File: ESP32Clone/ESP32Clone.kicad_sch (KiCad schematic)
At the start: 14 parts, among them J1 Connector, USB-TYPE-C-16P, U1 TPS54331DR

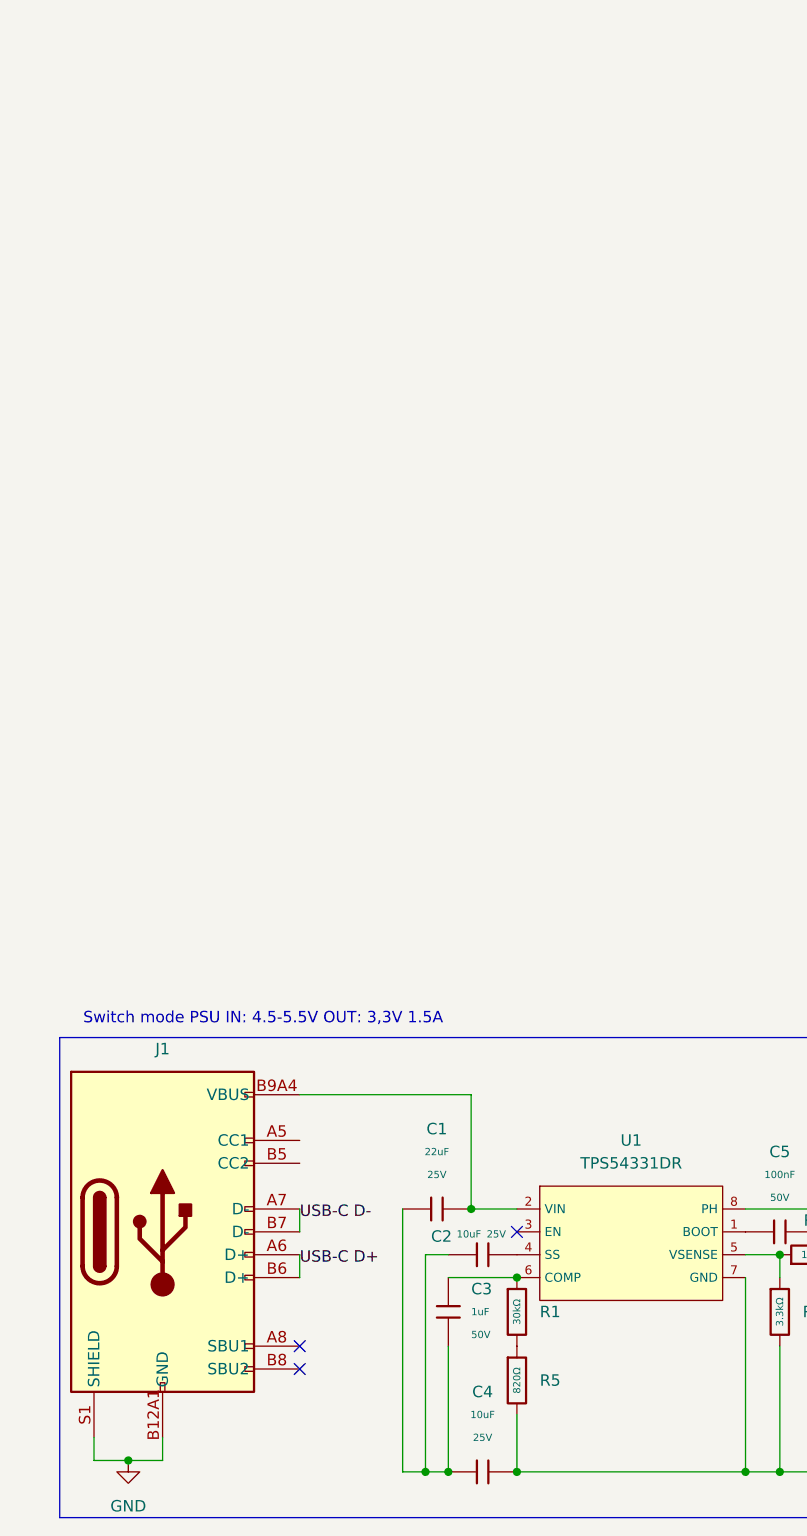
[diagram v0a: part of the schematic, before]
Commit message: connected configuration pins
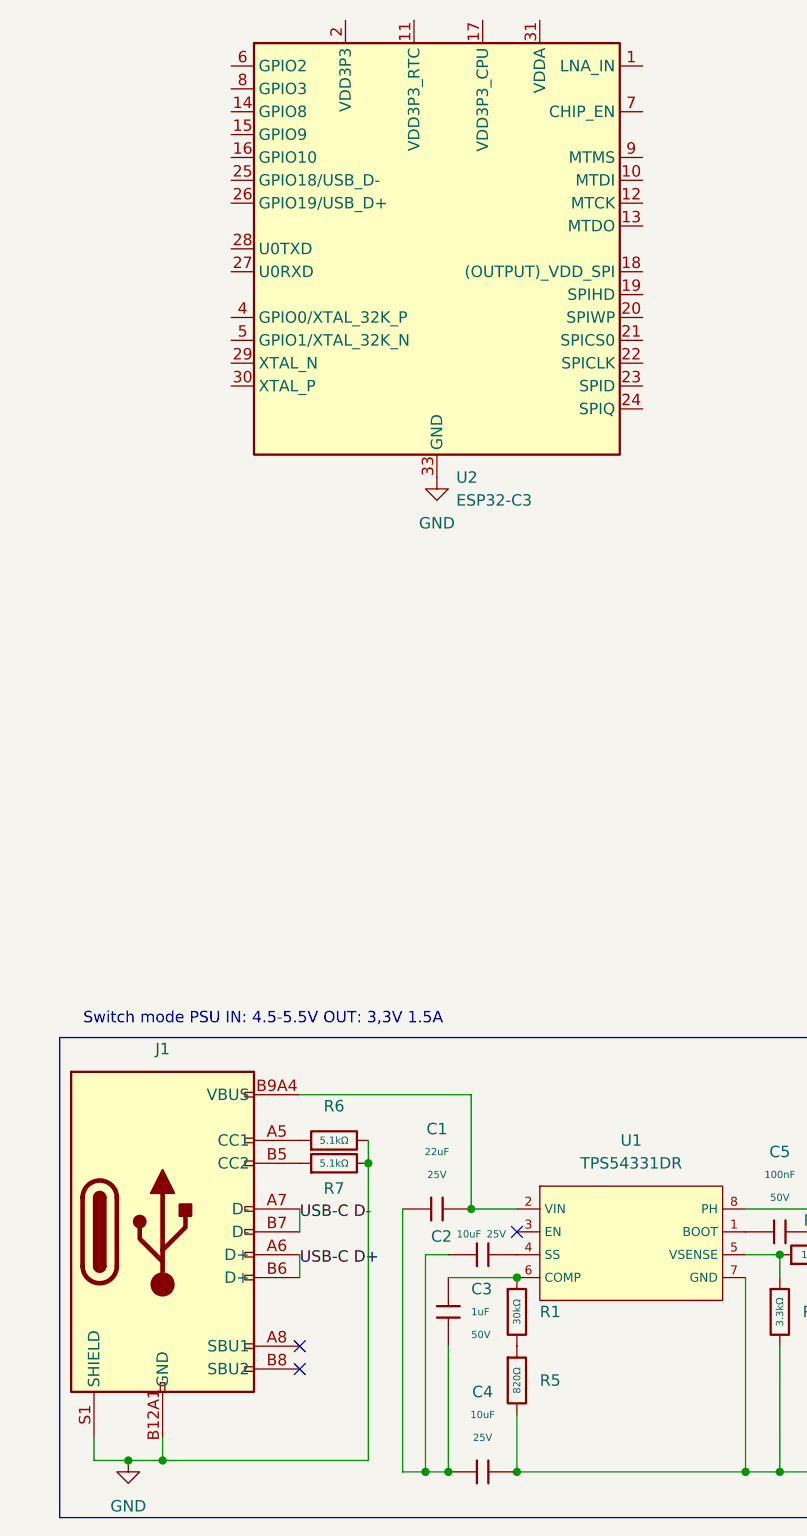
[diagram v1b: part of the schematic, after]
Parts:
- added R6, R7: 5.1kΩ, PCM_JLCPCB:R_0805, symbol PCM_JLCPCB-Resistors:0805,5.1kΩ
- added U2: ESP32-C3, PCM_JLCPCB:QFN-32-1EP_5x5mm_P0.5mm_EP3.7x3.7mm_ThermalVias, symbol PCM_JLCPCB-Extended:MCU, ESP32-C3
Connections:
- net GND: now also R6.2, R7.2, U2.33 (GND)
- net at J1.A5 (CC1): now also R6.1
- net at J1.B5 (CC2): now also R7.1
- new net: U2.2 (VDD3P3), U2.3 (VDD3P3)
- new net: U2.31 (VDDA), U2.32 (VDDA)

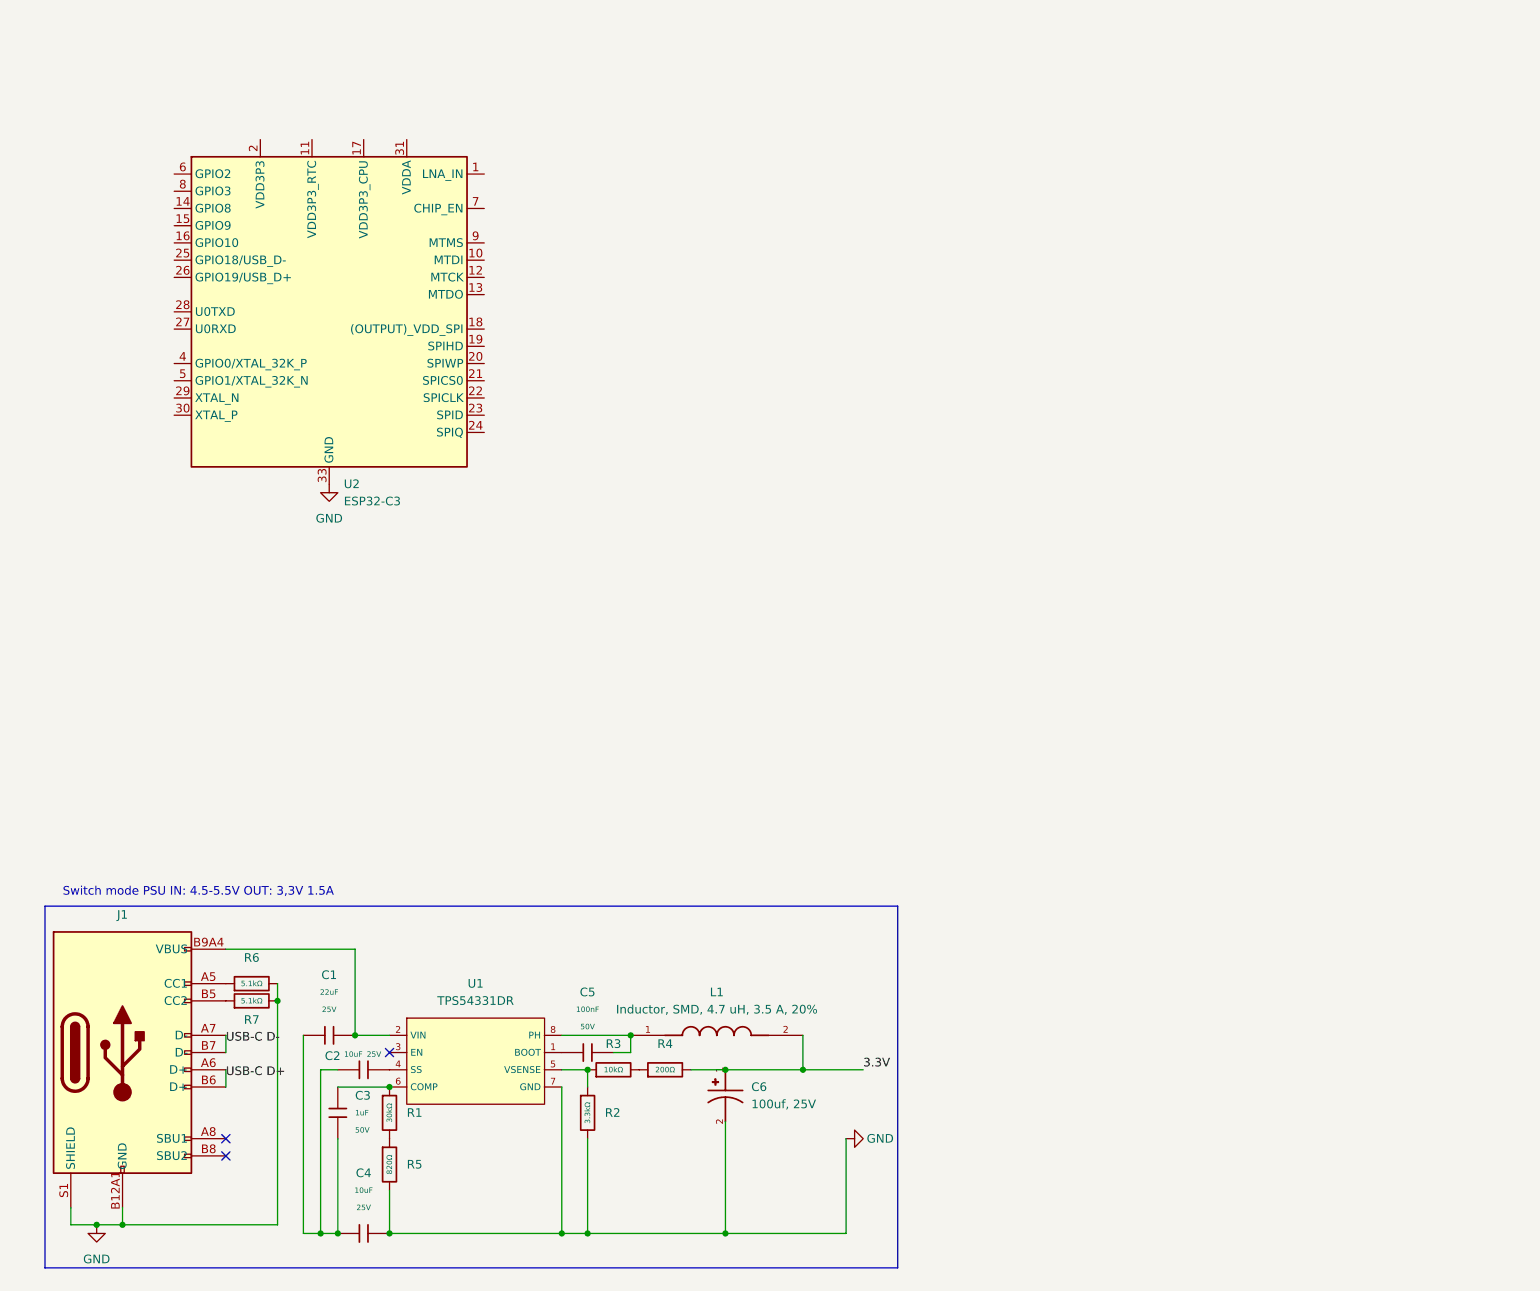
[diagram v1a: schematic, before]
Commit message: ESP 32 added
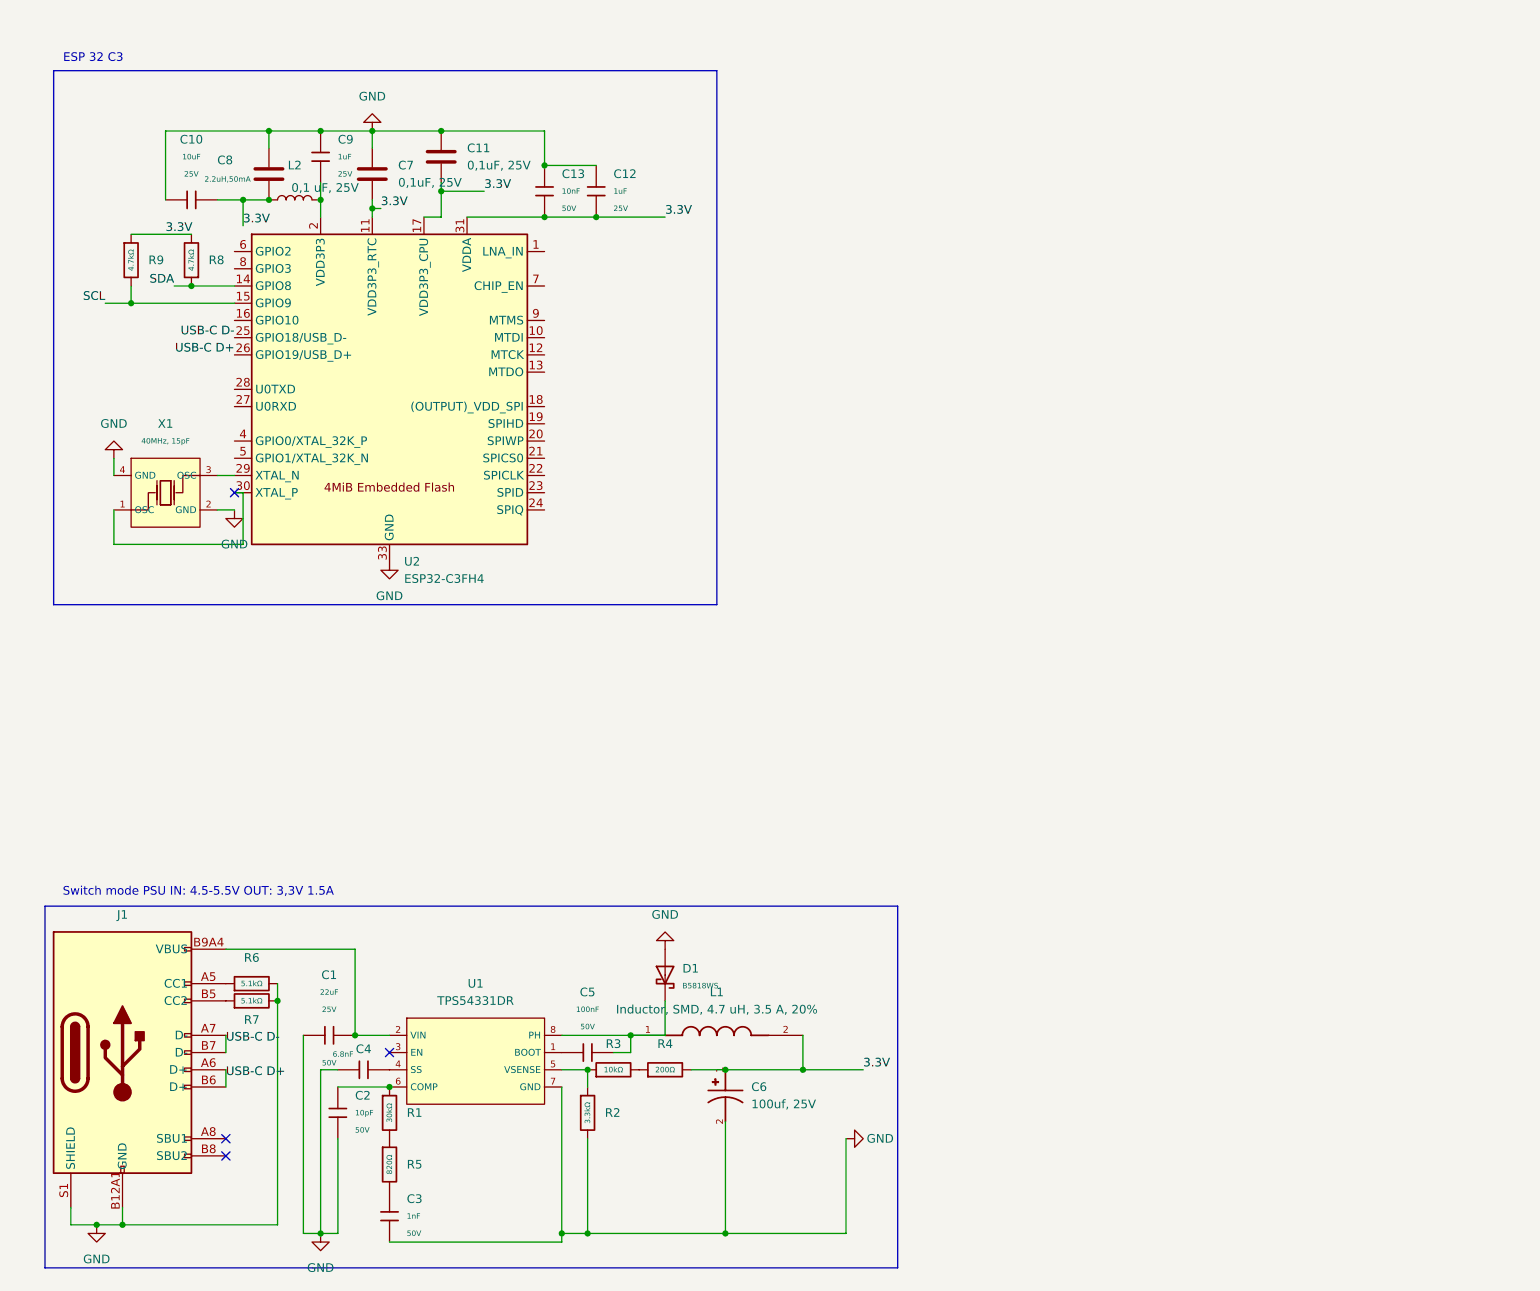
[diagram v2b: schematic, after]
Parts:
- removed C2, C4: 10uF, PCM_JLCPCB:C_0805, symbol PCM_JLCPCB-Capacitors:0805,10uF
- removed C3: 1uF, PCM_JLCPCB:C_0603, symbol PCM_JLCPCB-Capacitors:0603,1uF
- removed U2: ESP32-C3, PCM_JLCPCB:QFN-32-1EP_5x5mm_P0.5mm_EP3.7x3.7mm_ThermalVias, symbol PCM_JLCPCB-Extended:MCU, ESP32-C3
- added C10: 10uF, PCM_JLCPCB:C_0603, symbol PCM_JLCPCB-Capacitors:0603,10uF,(2)
- added C11, C7: 0,1uF, 25V, symbol Device:C
- added C12, C9: 1uF, PCM_JLCPCB:C_0402, symbol PCM_JLCPCB-Capacitors:0402,1uF
- added C13: 10nF, PCM_JLCPCB:C_0402, symbol PCM_JLCPCB-Capacitors:0402,10nF
- added C2: 10pF, PCM_JLCPCB:C_0402, symbol PCM_JLCPCB-Capacitors:0402,10pF
- added C3: 1nF, PCM_JLCPCB:C_0402, symbol PCM_JLCPCB-Capacitors:0402,1nF
- added C4: 6.8nF, PCM_JLCPCB:C_0402, symbol PCM_JLCPCB-Capacitors:0402,6.8nF
- added C8: 0,1 uF, 25V, symbol Device:C
- added D1: B5818WS, PCM_JLCPCB:D_SOD-323, symbol PCM_JLCPCB-Diodes:Schottky,B5818WS
- added L2: 2.2uH,50mA, PCM_JLCPCB:L_0805, symbol PCM_JLCPCB-Inductors:2.2uH,50mA
- added R8, R9: 4.7kΩ, PCM_JLCPCB:R_0805, symbol PCM_JLCPCB-Resistors:0805,4.7kΩ
- added U2: ESP32-C3FH4, PCM_JLCPCB:QFN-32-1EP_5x5mm_P0.5mm_EP3.7x3.7mm_ThermalVias, symbol PCM_JLCPCB-Extended:MCU, ESP32-C3FH4
- added X1: 40MHz, 15pF, PCM_JLCPCB:OSC-SMD_4P-L3.2-W2.5-BL_SIT8008BI, symbol PCM_JLCPCB-Extended:Crystal, 40MHz, 15pF
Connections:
- net 3.3V: now also C10.2, C11.2, C12.1, C13.2, C7.2, C8.2, L2.1, R8.2, R9.1, U2.11 (VDD3P3_RTC), U2.17 (VDD3P3_CPU), U2.31 (VDDA), U2.32 (VDDA)
- net GND: now also C1.1, C10.1, C11.1, C12.2, C13.1, C2.2, C3.1, C4.1, C7.1, C8.1, C9.1, D1.2, U2.33 (GND), X1.2 (GND), X1.4 (GND); no longer R5.2
- net USB-C D+: now also U2.26 (GPIO19/USB_D+)
- net USB-C D-: now also U2.25 (GPIO18/USB_D-)
- net at U1.4 (SS): now also C4.2
- net at R1.1, U1.6 (COMP): now also C2.1
- net at C5.1, L1.1, U1.8 (PH): now also D1.1
- new net: C3.2, R5.2
- new net: C9.2, L2.2, U2.2 (VDD3P3), U2.3 (VDD3P3)
- new net: U2.29 (XTAL_N), X1.3 (OSC)
- new net: U2.30 (XTAL_P), X1.1 (OSC)
- new net SCL: R9.2, U2.15 (GPIO9)
- new net SDA: R8.1, U2.14 (GPIO8)
- no-connect marks 3 -> 4
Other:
- note added: "ESP 32 C3"

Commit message: Further work on connectors
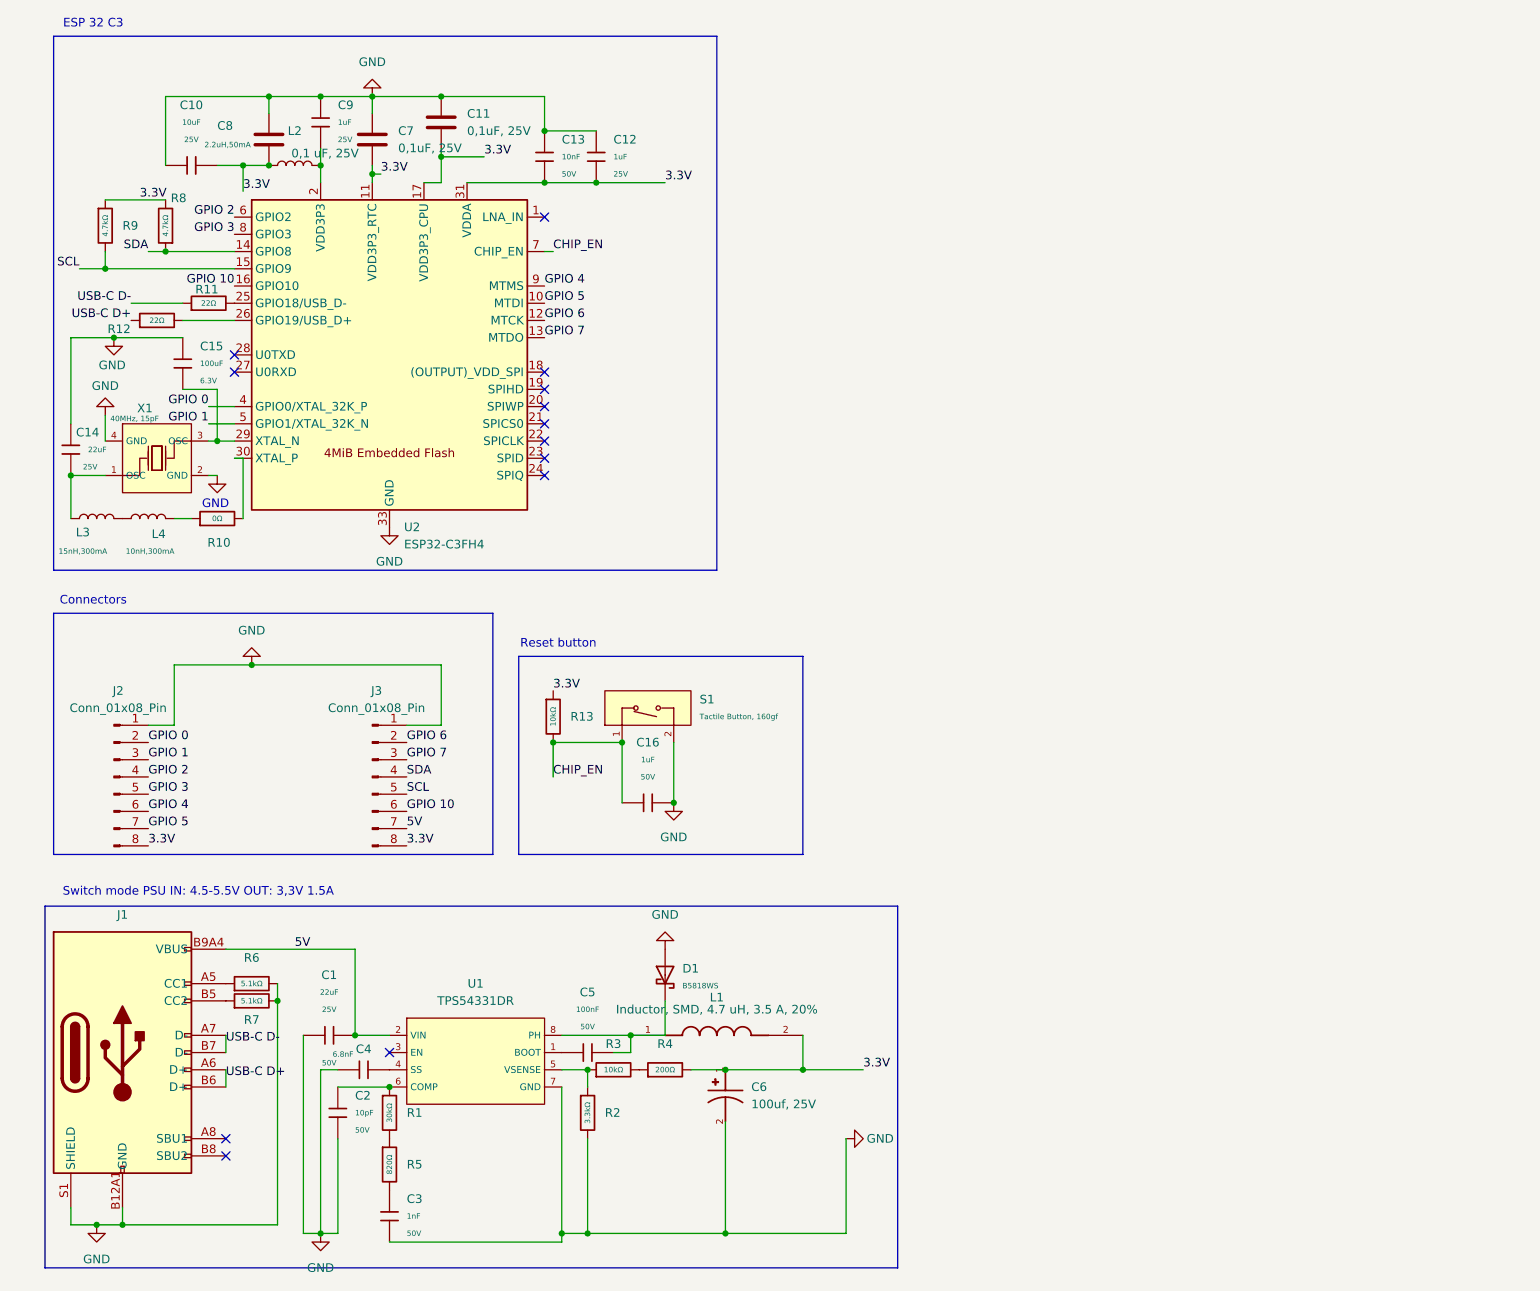
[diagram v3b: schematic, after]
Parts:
- added C14: 22uF, PCM_JLCPCB:C_0805, symbol PCM_JLCPCB-Capacitors:0805,22uF
- added C15: 100uF, PCM_JLCPCB:C_1206, symbol PCM_JLCPCB-Capacitors:1206,100uF
- added C16: 1uF, PCM_JLCPCB:C_0603, symbol PCM_JLCPCB-Capacitors:0603,1uF
- added J2, J3: Conn_01x08_Pin, symbol Connector:Conn_01x08_Pin
- added L3: 15nH,300mA, PCM_JLCPCB:L_0402, symbol PCM_JLCPCB-Inductors:15nH,300mA
- added L4: 10nH,300mA, PCM_JLCPCB:L_0402, symbol PCM_JLCPCB-Inductors:10nH,300mA
- added R10: 0Ω, PCM_JLCPCB:R_0805, symbol PCM_JLCPCB-Resistors:0805,0Ω
- added R11, R12: 22Ω, PCM_JLCPCB:R_0805, symbol PCM_JLCPCB-Resistors:0805,22Ω
- added R13: 10kΩ, PCM_JLCPCB:R_0603, symbol PCM_JLCPCB-Resistors:0603,10kΩ
- added S1: Tactile Button, 160gf, PCM_JLCPCB:SW_TS-1088-AR02016, symbol PCM_JLCPCB-Connectors_Buttons:Tactile Button, 160gf, 12V, 50mA, 4.0mm
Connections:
- net 3.3V: now also J2.8 (Pin_8), J3.8 (Pin_8), R13.1
- net GND: now also C14.1, C15.2, C16.2, J2.1 (Pin_1), J3.1 (Pin_1), S1.2 (B)
- net SCL: now also J3.5 (Pin_5)
- net SDA: now also J3.4 (Pin_4)
- net USB-C D+: now also R12.1; no longer U2.26 (GPIO19/USB_D+)
- net USB-C D-: now also R11.1; no longer U2.25 (GPIO18/USB_D-)
- net 5V: now reaches C1.2, J1.A9B4 (VBUS), J1.B9A4 (VBUS), U1.2 (VIN)
- net 5V: now also J3.7 (Pin_7)
- net GPIO 5: now reaches U2.10 (MTDI)
- net GPIO 5: now also J2.7 (Pin_7)
- net GPIO 6: now reaches U2.12 (MTCK)
- net GPIO 6: now also J3.2 (Pin_2)
- net GPIO 7: now reaches U2.13 (MTDO)
- net GPIO 7: now also J3.3 (Pin_3)
- net GPIO 10: now reaches U2.16 (GPIO10)
- net GPIO 10: now also J3.6 (Pin_6)
- net at U2.29 (XTAL_N), X1.3 (OSC): now also C15.1
- net at U2.30 (XTAL_P): now also R10.2; no longer X1.1 (OSC)
- net GPIO 0: now reaches U2.4 (GPIO0/XTAL_32K_P)
- net GPIO 0: now also J2.2 (Pin_2)
- net GPIO 1: now reaches U2.5 (GPIO1/XTAL_32K_N)
- net GPIO 1: now also J2.3 (Pin_3)
- net GPIO 2: now reaches U2.6 (GPIO2)
- net GPIO 2: now also J2.4 (Pin_4)
- net CHIP_EN: now reaches U2.7 (CHIP_EN)
- net CHIP_EN: now also C16.1, R13.2, S1.1 (A)
- net GPIO 3: now reaches U2.8 (GPIO3)
- net GPIO 3: now also J2.5 (Pin_5)
- net GPIO 4: now reaches U2.9 (MTMS)
- net GPIO 4: now also J2.6 (Pin_6)
- new net: L4.2, R10.1
- new net: R12.2, U2.26 (GPIO19/USB_D+)
- new net: R11.2, U2.25 (GPIO18/USB_D-)
- new net: C14.2, L3.1, X1.1 (OSC)
- new net: L3.2, L4.1
- no-connect marks 4 -> 13
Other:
- note added: "Connectors"
- note added: "GND"
- note added: "Reset button"
- moved on the sheet: C10, C11, C12, C13, C7, C8, C9, L2, R8, R9, U2, X1
